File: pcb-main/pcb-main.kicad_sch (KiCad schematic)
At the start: 36 parts, among them J1 AVR-ISP-6, J2 Conn_02x06_Counter_Clockwise, M1 Stepper_Motor, SW1 SW_MEC_5E, U1 ATmega328P-AU, U2 HT1621B-LQFP-A, U3 VIM878, U4 PCF8563T, Y1 16MHz, Y2 32kHz

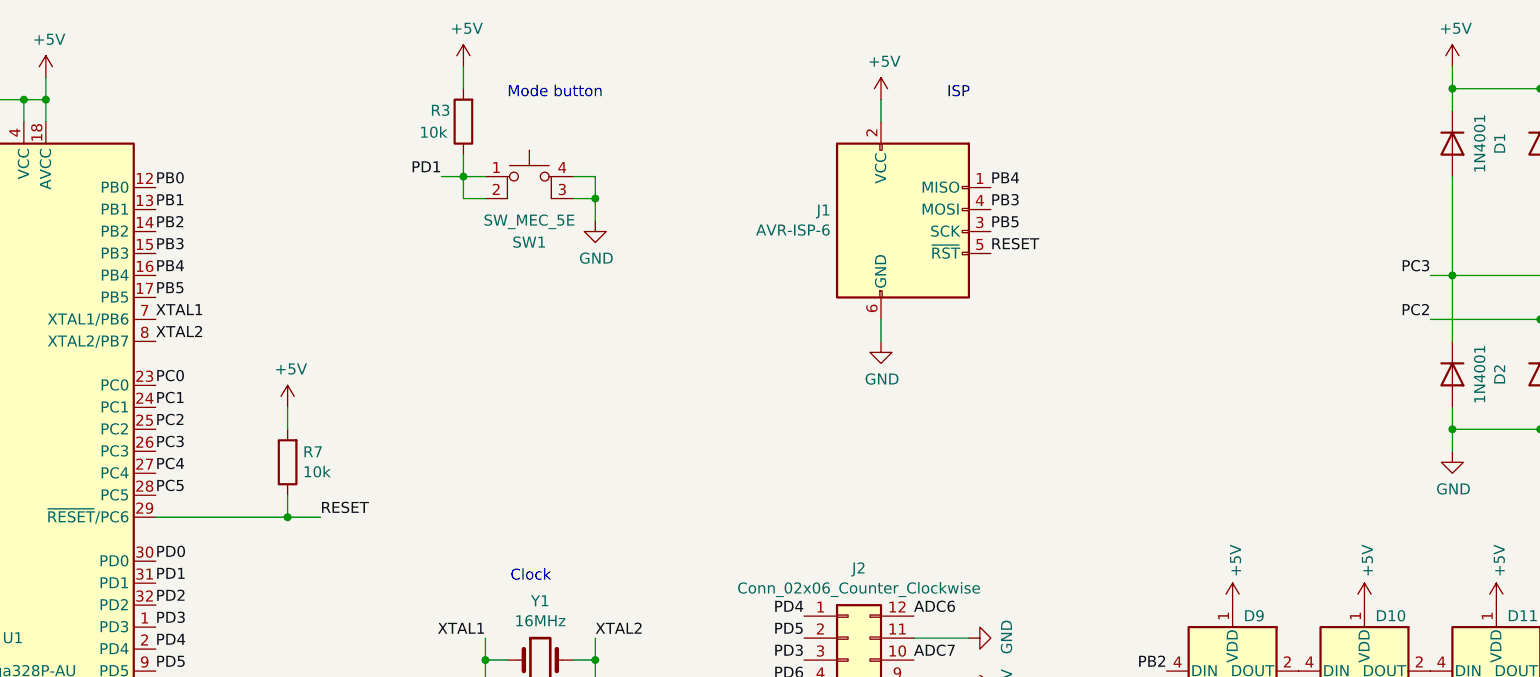
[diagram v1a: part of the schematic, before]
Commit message: resolves #21: reset button
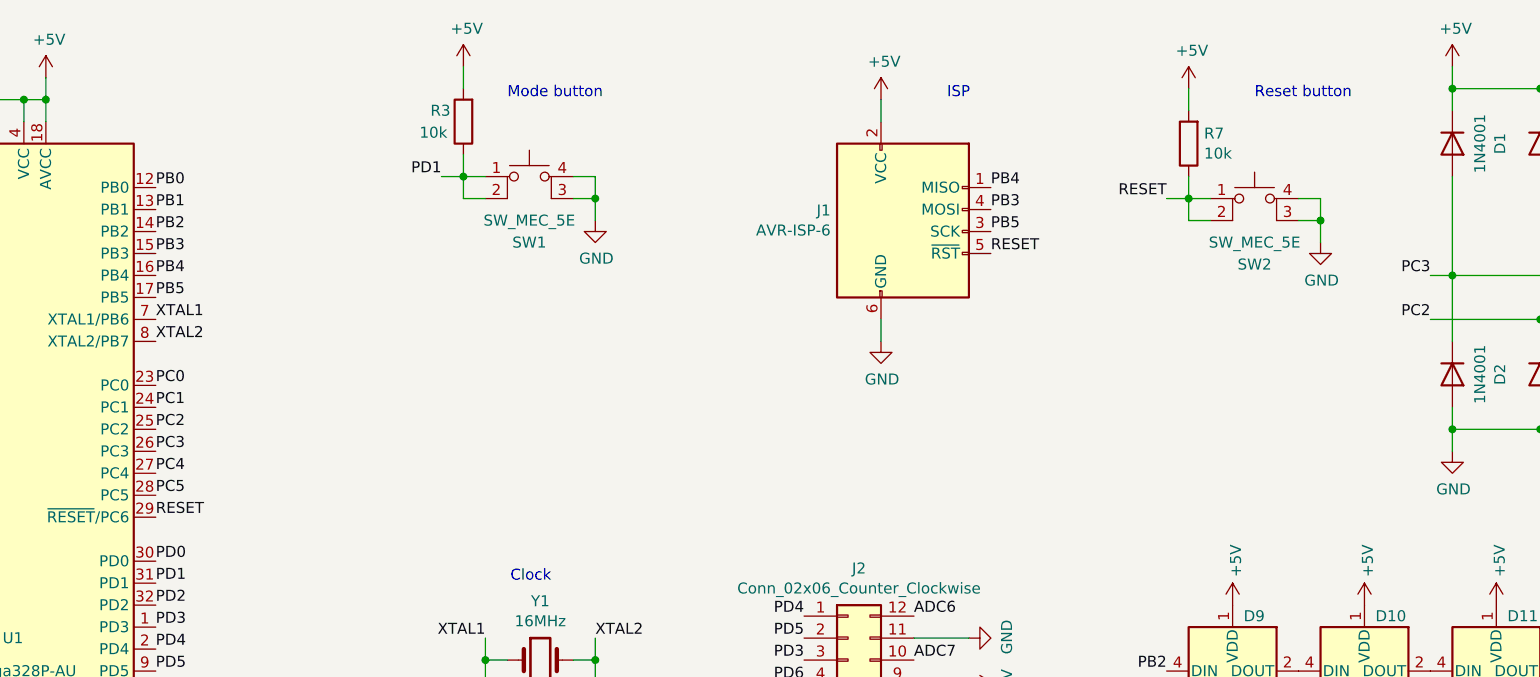
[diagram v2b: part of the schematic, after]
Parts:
- added SW2: SW_MEC_5E, footprints:TS_1187A, symbol Switch:SW_MEC_5E
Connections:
- net GND: now also SW2.3 (K), SW2.4 (A)
- net RESET: now also SW2.1, SW2.2
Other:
- note added: "Reset button"
- moved on the sheet: R7
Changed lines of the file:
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@@
   (junction (at 105.41 102.87) (diameter 0) (color 0 0 0 0)
   )
+  (junction (at 201.93 39.37) (diameter 0) (color 0 0 0 0)
+  )
   (junction (at 34.29 25.4) (diameter 0) (color 0 0 0 0)
   )
@@
   (junction (at 217.17 45.72) (diameter 0) (color 0 0 0 0)
   )
-  (junction (at 82.55 73.66) (diameter 0) (color 0 0 0 0)
-  )
   (junction (at 262.89 24.13) (diameter 0) (color 0 0 0 0)
   )
@@
   (junction (at 227.33 63.5) (diameter 0) (color 0 0 0 0)
   )
+  (junction (at 186.69 36.83) (diameter 0) (color 0 0 0 0)
+  )
   (junction (at 34.29 161.29) (diameter 0) (color 0 0 0 0)
   )
@@
     (stroke (width 0) (type default) (color 0 0 0 0))
   )
+  (wire (pts (xy 186.69 36.83) (xy 186.69 39.37))
+    (stroke (width 0) (type default) (color 0 0 0 0))
+  )
   (wire (pts (xy 262.89 39.37) (xy 262.89 34.29))
     (stroke (width 0) (type default) (color 0 0 0 0))
   )
+  (wire (pts (xy 201.93 39.37) (xy 201.93 41.91))
+    (stroke (width 0) (type default) (color 0 0 0 0))
+  )
   (wire (pts (xy 151.13 50.8) (xy 151.13 53.34))
     (stroke (width 0) (type default) (color 0 0 0 0))
   )
-  (wire (pts (xy 82.55 63.5) (xy 82.55 60.96))
+  (wire (pts (xy 186.69 26.67) (xy 186.69 24.13))
     (stroke (width 0) (type default) (color 0 0 0 0))
   )
@@
     (stroke (width 0) (type default) (color 0 0 0 0))
   )
-  (wire (pts (xy 86.36 73.66) (xy 82.55 73.66))
-    (stroke (width 0) (type default) (color 0 0 0 0))
-  )
   (wire (pts (xy 118.11 36.83) (xy 118.11 39.37))
     (stroke (width 0) (type default) (color 0 0 0 0))
@@
     (stroke (width 0) (type default) (color 0 0 0 0))
   )
+  (wire (pts (xy 186.69 39.37) (xy 189.23 39.37))
+    (stroke (width 0) (type default) (color 0 0 0 0))
+  )
   (wire (pts (xy 34.29 176.53) (xy 34.29 173.99))
     (stroke (width 0) (type default) (color 0 0 0 0))
@@
     (stroke (width 0) (type default) (color 0 0 0 0))
   )
-  (wire (pts (xy 82.55 73.66) (xy 67.31 73.66))
-    (stroke (width 0) (type default) (color 0 0 0 0))
-  )
   (wire (pts (xy 118.11 87.63) (xy 118.11 90.17))
     (stroke (width 0) (type default) (color 0 0 0 0))
@@
     (stroke (width 0) (type default) (color 0 0 0 0))
   )
-  (wire (pts (xy 82.55 71.12) (xy 82.55 73.66))
-    (stroke (width 0) (type default) (color 0 0 0 0))
-  )
   (wire (pts (xy 195.58 137.16) (xy 195.58 135.89))
     (stroke (width 0) (type default) (color 0 0 0 0))
@@
     (stroke (width 0) (type default) (color 0 0 0 0))
   )
+  (wire (pts (xy 199.39 36.83) (xy 201.93 36.83))
+    (stroke (width 0) (type default) (color 0 0 0 0))
+  )
+  (wire (pts (xy 201.93 39.37) (xy 201.93 36.83))
+    (stroke (width 0) (type default) (color 0 0 0 0))
+  )
   (wire (pts (xy 105.41 100.33) (xy 105.41 102.87))
     (stroke (width 0) (type default) (color 0 0 0 0))
@@
     (stroke (width 0) (type default) (color 0 0 0 0))
   )
+  (wire (pts (xy 186.69 36.83) (xy 189.23 36.83))
+    (stroke (width 0) (type default) (color 0 0 0 0))
+  )
   (wire (pts (xy 118.11 90.17) (xy 115.57 90.17))
     (stroke (width 0) (type default) (color 0 0 0 0))
@@
     (stroke (width 0) (type default) (color 0 0 0 0))
   )
+  (wire (pts (xy 186.69 34.29) (xy 186.69 36.83))
+    (stroke (width 0) (type default) (color 0 0 0 0))
+  )
   (wire (pts (xy 227.33 34.29) (xy 227.33 50.8))
     (stroke (width 0) (type default) (color 0 0 0 0))
@@
     (stroke (width 0) (type default) (color 0 0 0 0))
   )
+  (wire (pts (xy 184.15 36.83) (xy 186.69 36.83))
+    (stroke (width 0) (type default) (color 0 0 0 0))
+  )
   (wire (pts (xy 227.33 50.8) (xy 214.63 50.8))
     (stroke (width 0) (type default) (color 0 0 0 0))
@@
     (stroke (width 0) (type default) (color 0 0 0 0))
   )
+  (wire (pts (xy 199.39 39.37) (xy 201.93 39.37))
+    (stroke (width 0) (type default) (color 0 0 0 0))
+  )
   (wire (pts (xy 102.87 36.83) (xy 105.41 36.83))
     (stroke (width 0) (type default) (color 0 0 0 0))
@@
     (stroke (width 0) (type default) (color 0 0 0 0))
   )
+  (text "Reset button" (at 194.31 25.4 0)
+    (effects (font (size 1.27 1.27)) (justify left bottom))
+  )
   (text "ISP" (at 158.75 25.4 0)
     (effects (font (size 1.27 1.27)) (justify left bottom))
@@
     (effects (font (size 1.27 1.27)) (justify left bottom))
   )
+  (label "RESET" (at 184.15 36.83 180)
+    (effects (font (size 1.27 1.27)) (justify right bottom))
+  )
   (label "PB3" (at 67.31 43.18 0)
     (effects (font (size 1.27 1.27)) (justify left bottom))
@@
     (effects (font (size 1.27 1.27)) (justify left bottom))
   )
-  (label "RESET" (at 86.36 73.66 0)
+  (label "RESET" (at 67.31 73.66 0)
     (effects (font (size 1.27 1.27)) (justify left bottom))
   )
@@
     (pin "1")
   )
-  (symbol (lib_id "power:+5V") (at 82.55 60.96 0) (unit 1)
-    (in_bom yes) (on_board yes)
-    (property "Reference" "#PWR0114" (id 0) (at 82.55 64.77 0)
-      (effects (font (size 1.27 1.27)) hide)
-    )
-    (property "Value" "+5V" (id 1) (at 82.931 56.5658 0))
-    (property "Footprint" "" (id 2) (at 82.55 60.96 0)
-      (effects (font (size 1.27 1.27)) hide)
-    )
-    (property "Datasheet" "" (id 3) (at 82.55 60.96 0)
-      (effects (font (size 1.27 1.27)) hide)
-    )
-    (pin "1")
-  )
-  (symbol (lib_id "Device:R") (at 82.55 67.31 180) (unit 1)
-    (in_bom yes) (on_board yes)
-    (property "Reference" "R7" (id 0) (at 84.328 66.1416 0)
+  (symbol (lib_id "power:+5V") (at 186.69 24.13 0) (unit 1)
+    (in_bom yes) (on_board yes)
+    (property "Reference" "#PWR0114" (id 0) (at 186.69 27.94 0)
+      (effects (font (size 1.27 1.27)) hide)
+    )
+    (property "Value" "+5V" (id 1) (at 187.071 19.7358 0))
+    (property "Footprint" "" (id 2) (at 186.69 24.13 0)
+      (effects (font (size 1.27 1.27)) hide)
+    )
+    (property "Datasheet" "" (id 3) (at 186.69 24.13 0)
+      (effects (font (size 1.27 1.27)) hide)
+    )
+    (pin "1")
+  )
+  (symbol (lib_id "Device:R") (at 186.69 30.48 180) (unit 1)
+    (in_bom yes) (on_board yes)
+    (property "Reference" "R7" (id 0) (at 188.468 29.3116 0)
       (effects (font (size 1.27 1.27)) (justify right))
     )
-    (property "Value" "10k" (id 1) (at 84.328 68.453 0)
+    (property "Value" "10k" (id 1) (at 188.468 31.623 0)
       (effects (font (size 1.27 1.27)) (justify right))
     )
-    (property "Footprint" "Resistor_SMD:R_1206_3216Metric_Pad1.30x1.75mm_HandSolder" (id 2) (at 84.328 67.31 90)
-      (effects (font (size 1.27 1.27)) hide)
-    )
-    (property "Datasheet" "~" (id 3) (at 82.55 67.31 0)
+    (property "Footprint" "Resistor_SMD:R_1206_3216Metric_Pad1.30x1.75mm_HandSolder" (id 2) (at 188.468 30.48 90)
+      (effects (font (size 1.27 1.27)) hide)
+    )
+    (property "Datasheet" "~" (id 3) (at 186.69 30.48 0)
       (effects (font (size 1.27 1.27)) hide)
     )
@@
     (pin "1")
   )
+  (symbol (lib_id "power:GND") (at 201.93 41.91 0) (unit 1)
+    (in_bom yes) (on_board yes)
+    (property "Reference" "#PWR0134" (id 0) (at 201.93 48.26 0)
+      (effects (font (size 1.27 1.27)) hide)
+    )
+    (property "Value" "GND" (id 1) (at 202.057 46.3042 0))
+    (property "Footprint" "" (id 2) (at 201.93 41.91 0)
+      (effects (font (size 1.27 1.27)) hide)
+    )
+    (property "Datasheet" "" (id 3) (at 201.93 41.91 0)
+      (effects (font (size 1.27 1.27)) hide)
+    )
+    (pin "1")
+  )
+  (symbol (lib_id "Switch:SW_MEC_5E") (at 194.31 39.37 0) (unit 1)
+    (in_bom yes) (on_board yes)
+    (property "Reference" "SW2" (id 0) (at 194.31 44.45 0))
+    (property "Value" "SW_MEC_5E" (id 1) (at 194.31 41.91 0))
+    (property "Footprint" "footprints:TS_1187A" (id 2) (at 194.31 31.75 0)
+      (effects (font (size 1.27 1.27)) hide)
+    )
+    (property "Datasheet" "http://www.apem.com/int/index.php?controller=attachment&id_attachment=1371" (id 3) (at 194.31 31.75 0)
+      (effects (font (size 1.27 1.27)) hide)
+    )
+    (property "LCSC" "C318884" (id 4) (at 194.31 39.37 0)
+      (effects (font (size 1.27 1.27)) hide)
+    )
+    (pin "1")
+    (pin "2")
+    (pin "3")
+    (pin "4")
+  )
   (sheet_instances
     (path "/" (page "1"))
@@
       (reference "#PWR0133") (unit 1) (value "GND") (footprint "")
     )
+    (path "/e5f059b7-543a-4d01-a839-135527104101"
+      (reference "#PWR0134") (unit 1) (value "GND") (footprint "")
+    )
     (path "/00000000-0000-0000-0000-000061a65214"
       (reference "BT1") (unit 1) (value "Battery_Cell") (footprint "footprints:CR1220")
@@
       (reference "SW1") (unit 1) (value "SW_MEC_5E") (footprint "footprints:TS_1187A")
     )
+    (path "/ee69d709-4f6a-4766-a15a-1522a72adba3"
+      (reference "SW2") (unit 1) (value "SW_MEC_5E") (footprint "footprints:TS_1187A")
+    )
     (path "/00000000-0000-0000-0000-0000612e398c"
